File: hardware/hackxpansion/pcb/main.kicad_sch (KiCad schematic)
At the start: 4 parts

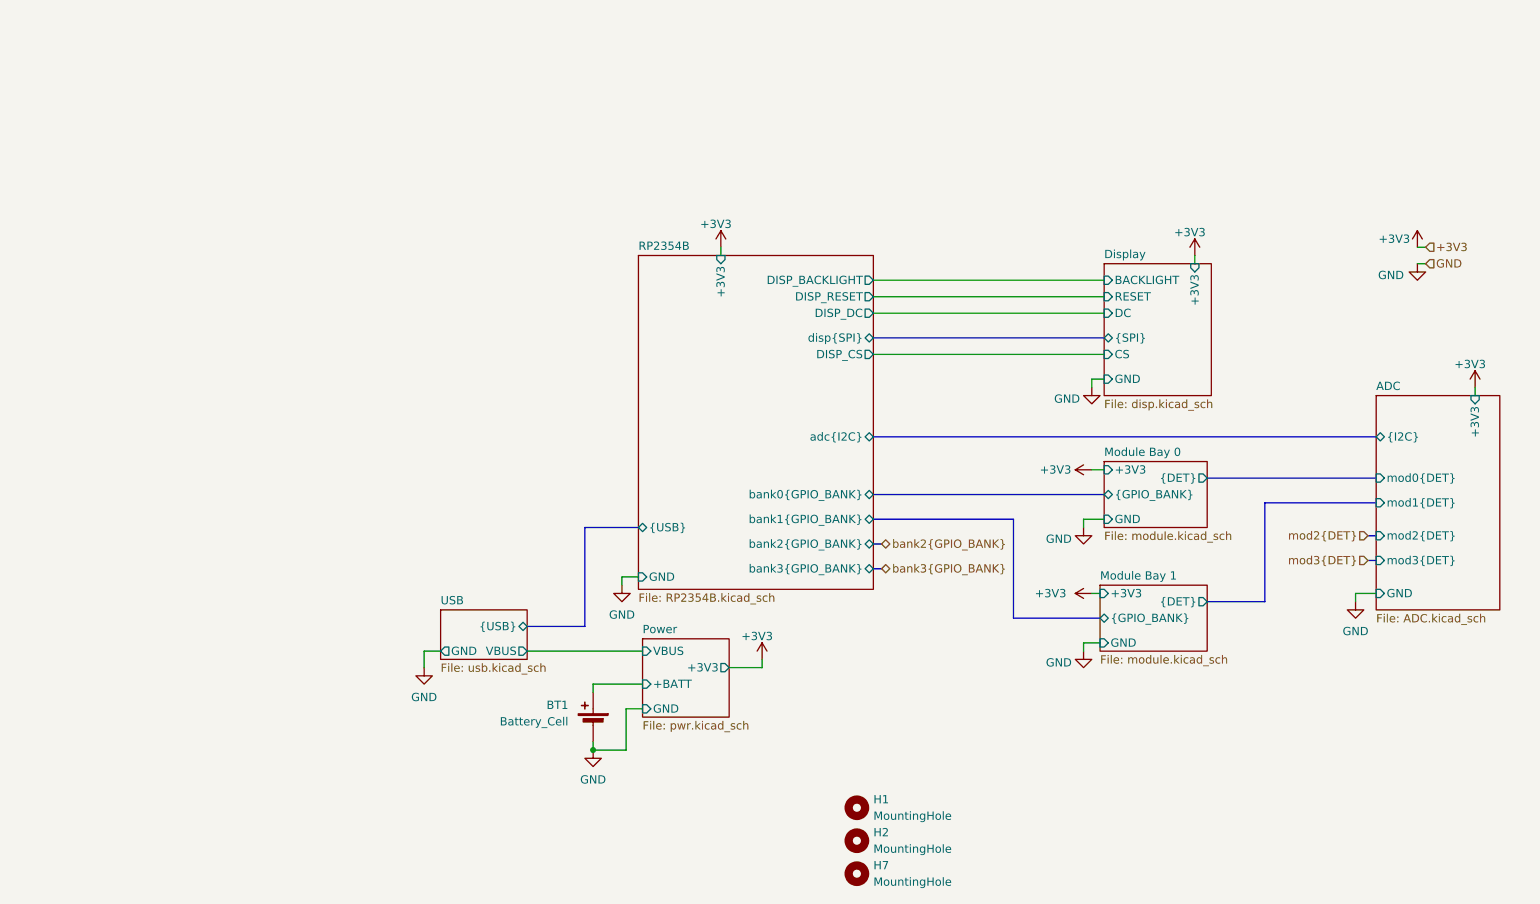
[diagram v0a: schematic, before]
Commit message: reordered shematic
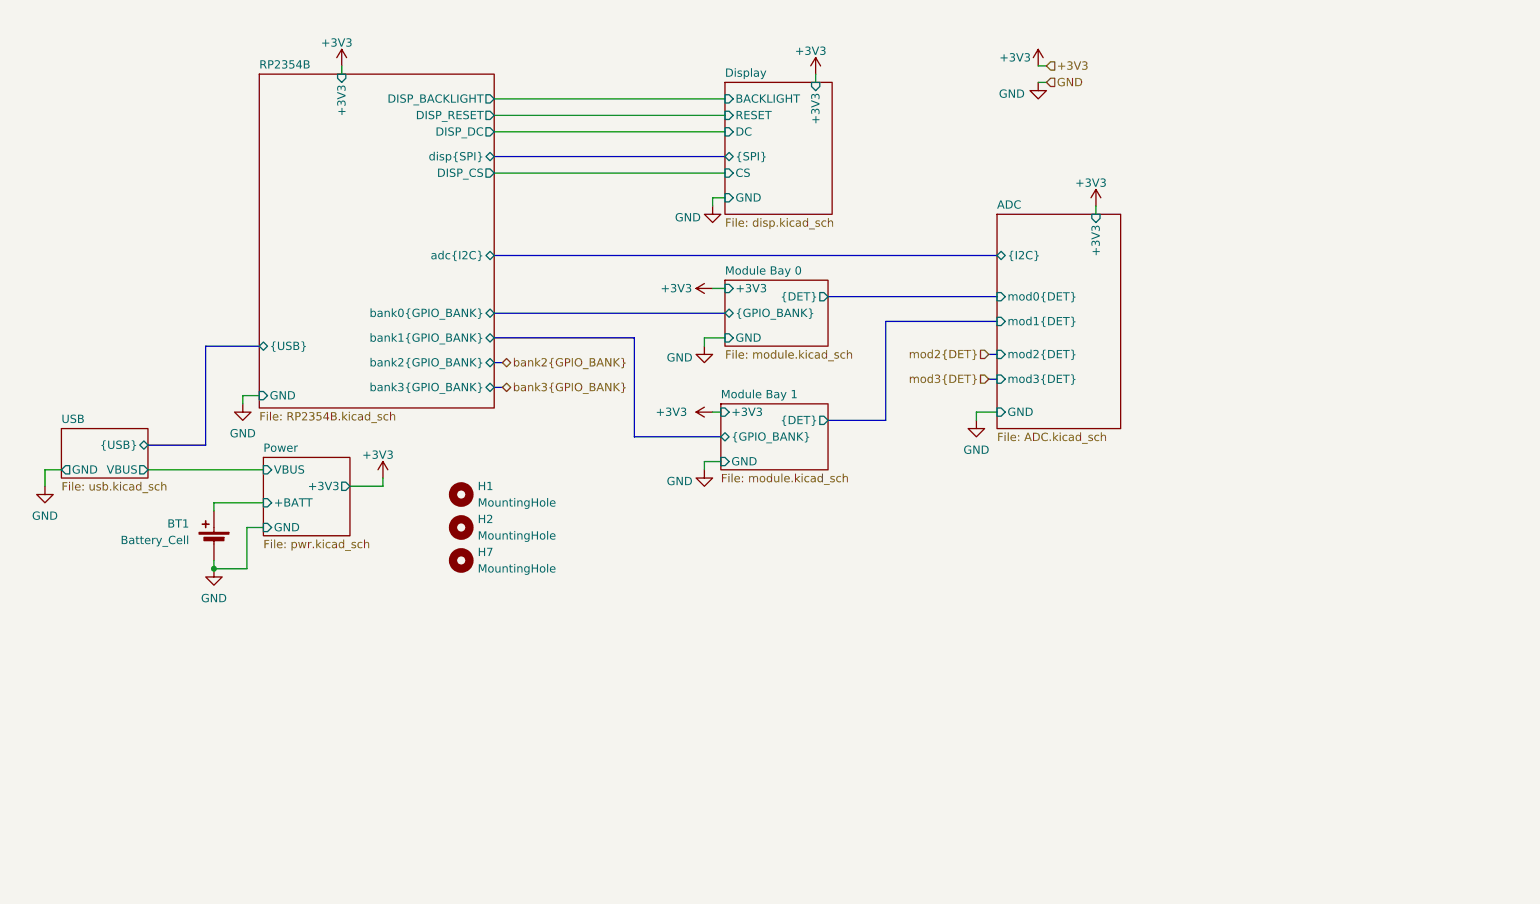
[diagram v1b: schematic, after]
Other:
- moved on the sheet: BT1, H1, H2, H7

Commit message: changed bom
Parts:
- BT1: LCSC C295747 -> C177225
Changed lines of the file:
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@@
 			)
 		)
-		(property "LCSC" "C295747"
+		(property "LCSC" "C177225"
 			(at 44.45 95.25 0)
 			(hide yes)

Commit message: switched battery connectory polarity
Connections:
- net GND: now also BT1.2 (-); no longer BT1.1 (-)
- net Power/+BATT: now also BT1.1 (+); no longer BT1.2 (+)

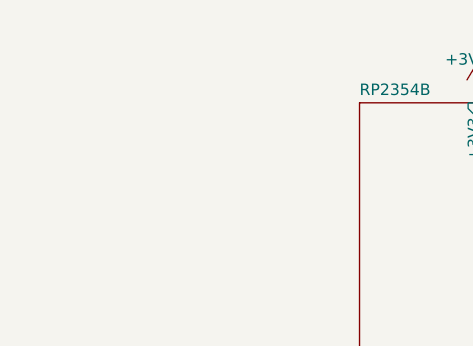
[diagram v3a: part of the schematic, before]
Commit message: added silkscreen
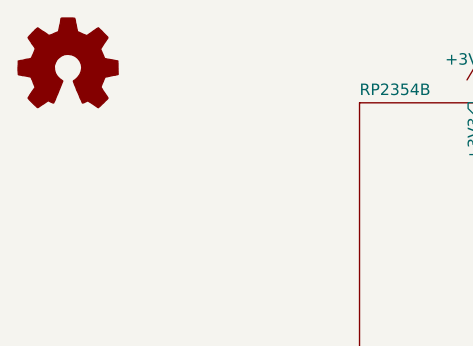
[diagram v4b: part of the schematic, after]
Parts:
- added SYM1: Logo_Open_Hardware_Small, Symbol:OSHW-Logo_5.7x6mm_SilkScreen, symbol Graphic:Logo_Open_Hardware_Small
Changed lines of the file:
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@@
+	)
+	(symbol
+		(lib_id "Graphic:Logo_Open_Hardware_Small")
+		(at 19.05 19.05 0)
+		(unit 1)
+		(body_style 1)
+		(exclude_from_sim no)
+		(in_bom no)
+		(on_board yes)
+		(in_pos_files yes)
+		(dnp no)
+		(fields_autoplaced yes)
+		(property "Reference" "SYM1"
+			(at 19.05 12.065 0)
+			(hide yes)
+			(show_name no)
+			(do_not_autoplace no)
+			(effects
+				(font
+					(size 1.27 1.27)
+				)
+			)
+		)
+		(property "Value" "Logo_Open_Hardware_Small"
+			(at 19.05 24.765 0)
+			(hide yes)
+			(show_name no)
+			(do_not_autoplace no)
+			(effects
+				(font
+					(size 1.27 1.27)
+				)
+			)
+		)
+		(property "Footprint" "Symbol:OSHW-Logo_5.7x6mm_SilkScreen"
+			(at 19.05 19.05 0)
+			(hide yes)
+			(show_name no)
+			(do_not_autoplace no)
+			(effects
+				(font
+					(size 1.27 1.27)
+				)
+			)
+		)
+		(property "Datasheet" ""
+			(at 19.05 19.05 0)
+			(hide yes)
+			(show_name no)
+			(do_not_autoplace no)
+			(effects
+				(font
+					(size 1.27 1.27)
+				)
+			)
+		)
+		(property "Description" "Open Hardware logo, small"
+			(at 19.05 19.05 0)
+			(hide yes)
+			(show_name no)
+			(do_not_autoplace no)
+			(effects
+				(font
+					(size 1.27 1.27)
+				)
+			)
+		)
+		(property "Sim.Enable" "0"
+			(at 19.05 19.05 0)
+			(hide yes)
+			(show_name no)
+			(do_not_autoplace no)
+			(effects
+				(font
+					(size 1.27 1.27)
+				)
+			)
+		)
+		(instances
+			(project "hackxpansion"
+				(path "/aaf5804d-3f78-442b-969e-39faa388db94/61af021d-ad04-487f-9d02-e2b100ecd1ae"
+					(reference "SYM1")
+					(unit 1)
+				)
+			)
+		)
 	)
 	(symbol
